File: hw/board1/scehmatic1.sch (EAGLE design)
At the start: 8 parts, among them IC1 LM317MBSTT3

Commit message: added brd file
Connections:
- new net N$2: C1.2
- net GND: no longer C1.2
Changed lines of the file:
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@@
 <part name="SUPPLY3" library="supply1" library_urn="urn:adsk.eagle:library:371" deviceset="GND" device=""/>
 <part name="R2" library="resistor" library_urn="urn:adsk.eagle:library:348" deviceset="R-US_" device="M0805" package3d_urn="urn:adsk.eagle:package:26079/1" value="4.4K"/>
-<part name="SUPPLY1" library="supply1" library_urn="urn:adsk.eagle:library:371" deviceset="GND" device=""/>
 <part name="SUPPLY2" library="supply1" library_urn="urn:adsk.eagle:library:371" deviceset="GND" device=""/>
 <part name="SUPPLY4" library="supply1" library_urn="urn:adsk.eagle:library:371" deviceset="GND" device=""/>
@@
 <attribute name="VALUE" x="45.212" y="41.91" size="1.778" layer="96" rot="MR180"/>
 </instance>
-<instance part="SUPPLY1" gate="1" x="15.24" y="30.48"/>
 <instance part="SUPPLY2" gate="1" x="58.42" y="30.48"/>
 <instance part="SUPPLY4" gate="1" x="73.66" y="30.48"/>
@@
 <wire x1="43.18" y1="35.56" x2="43.18" y2="33.02" width="0.1524" layer="91"/>
 <pinref part="R2" gate="G$1" pin="1"/>
-</segment>
-<segment>
-<pinref part="C1" gate="G$1" pin="2"/>
-<wire x1="15.24" y1="45.72" x2="15.24" y2="33.02" width="0.1524" layer="91"/>
-<pinref part="SUPPLY1" gate="1" pin="GND"/>
 </segment>
 </net>
@@
 </segment>
 </net>
+<net name="N$2" class="0">
+<segment>
+<pinref part="C1" gate="G$1" pin="2"/>
+<wire x1="15.24" y1="45.72" x2="15.24" y2="33.02" width="0.1524" layer="91"/>
+</segment>
+</net>

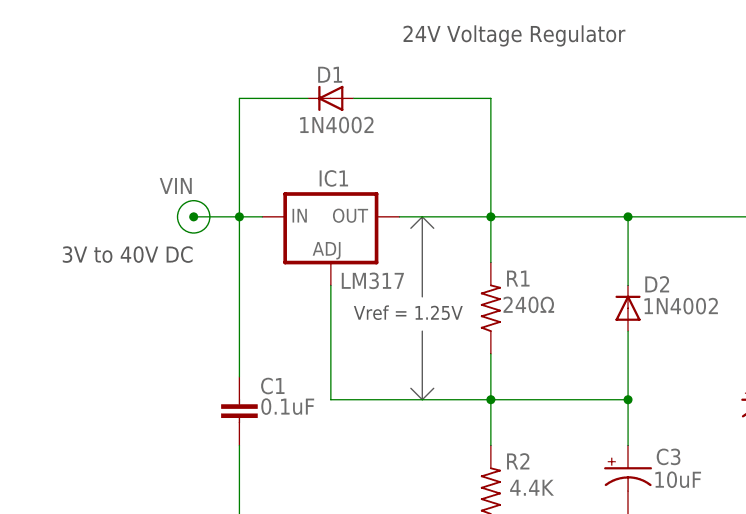
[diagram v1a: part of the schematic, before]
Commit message: deleted component from schematic and thus board
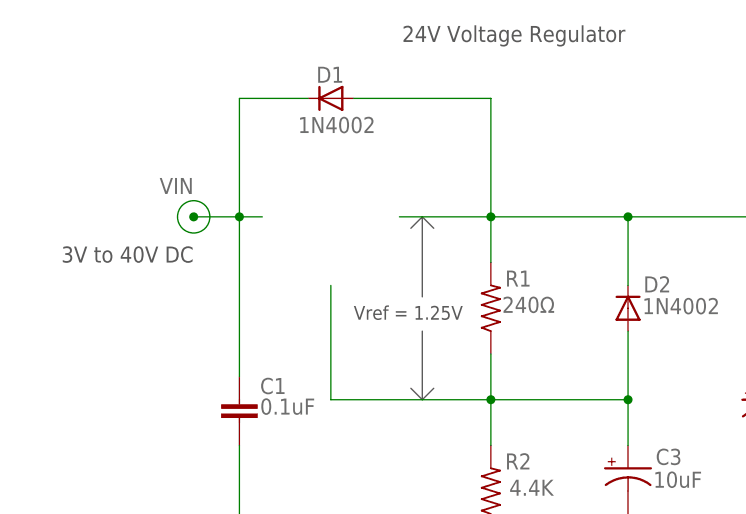
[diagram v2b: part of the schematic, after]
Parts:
- removed IC1: LM317MBSTT3, v-reg:LM317MBSTT3
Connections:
- net N$1: no longer IC1.ADJ
- net VIN: no longer IC1.IN
- net VO: no longer IC1.OUT
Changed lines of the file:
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@@
 </classes>
 <parts>
-<part name="IC1" library="v-reg" library_urn="urn:adsk.eagle:library:409" deviceset="LM317?*" device="MBSTT3" package3d_urn="urn:adsk.eagle:package:30370/1">
-<attribute name="PARTNUMBER" value="LM317"/>
-</part>
 <part name="R1" library="resistor" library_urn="urn:adsk.eagle:library:348" deviceset="R-US_" device="M0805" package3d_urn="urn:adsk.eagle:package:26079/1" value="240Ω"/>
 <part name="C1" library="rcl" library_urn="urn:adsk.eagle:library:334" deviceset="C-EU" device="075-052X106" package3d_urn="urn:adsk.eagle:package:23650/1" value="0.1uF"/>
@@
 </plain>
 <instances>
-<instance part="IC1" gate="G$1" x="25.4" y="71.12" smashed="yes">
-<attribute name="NAME" x="23.94" y="74.5" size="1.778" layer="95"/>
-<attribute name="VALUE" x="25.94" y="60.96" size="1.778" layer="96" display="off"/>
-<attribute name="PARTNUMBER" x="26.4" y="63.12" size="1.778" layer="96"/>
-</instance>
 <instance part="R1" gate="G$1" x="43.18" y="60.96" smashed="yes" rot="R90">
 <attribute name="NAME" x="47.6814" y="65.15" size="1.778" layer="95" rot="R180"/>
@@
 <wire x1="58.42" y1="45.72" x2="58.42" y2="50.8" width="0.1524" layer="91"/>
 <junction x="58.42" y="50.8"/>
-<pinref part="IC1" gate="G$1" pin="ADJ"/>
 <wire x1="25.4" y1="63.5" x2="25.4" y2="50.8" width="0.1524" layer="91"/>
 <wire x1="43.18" y1="50.8" x2="25.4" y2="50.8" width="0.1524" layer="91"/>
@@
 <wire x1="58.42" y1="71.12" x2="58.42" y2="63.5" width="0.1524" layer="91"/>
 <wire x1="58.42" y1="71.12" x2="73.66" y2="71.12" width="0.1524" layer="91"/>
-<pinref part="IC1" gate="G$1" pin="OUT"/>
 <pinref part="R1" gate="G$1" pin="2"/>
 <wire x1="73.66" y1="71.12" x2="78.74" y2="71.12" width="0.1524" layer="91"/>
@@
 <segment>
 <pinref part="C1" gate="G$1" pin="1"/>
-<pinref part="IC1" gate="G$1" pin="IN"/>
 <wire x1="17.78" y1="71.12" x2="15.24" y2="71.12" width="0.1524" layer="91"/>
 <wire x1="15.24" y1="71.12" x2="15.24" y2="53.34" width="0.1524" layer="91"/>
